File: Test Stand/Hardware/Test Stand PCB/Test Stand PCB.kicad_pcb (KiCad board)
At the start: 2 copper layers, 18 parts, among them J1 Screw_Terminal_01x02, J2 Screw_Terminal_01x02, J3 Screw_Terminal_01x02, J4 Screw_Terminal_01x04, J5 Screw_Terminal_01x02, U1 AdafruitHuzzah32Breakout, U2 Adafruit_MAX31856, U3 Adafruit_MAX31856, U4 Adafruit_MAX31856, U5 Adafruit_MAX31856, U7 INA_122P, U8 Adafruit_MicroSD_Breakout

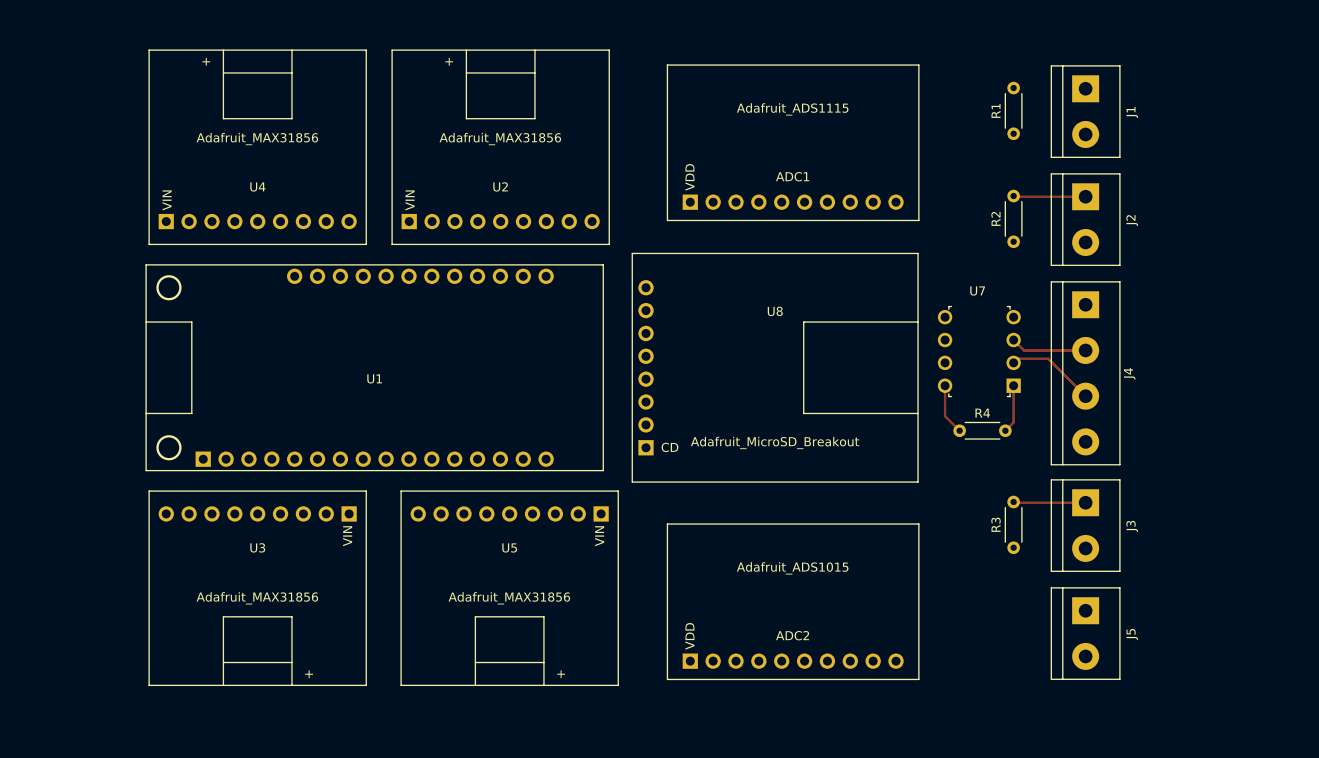
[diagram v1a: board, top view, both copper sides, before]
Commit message: Updated Test schematic and PCB Design
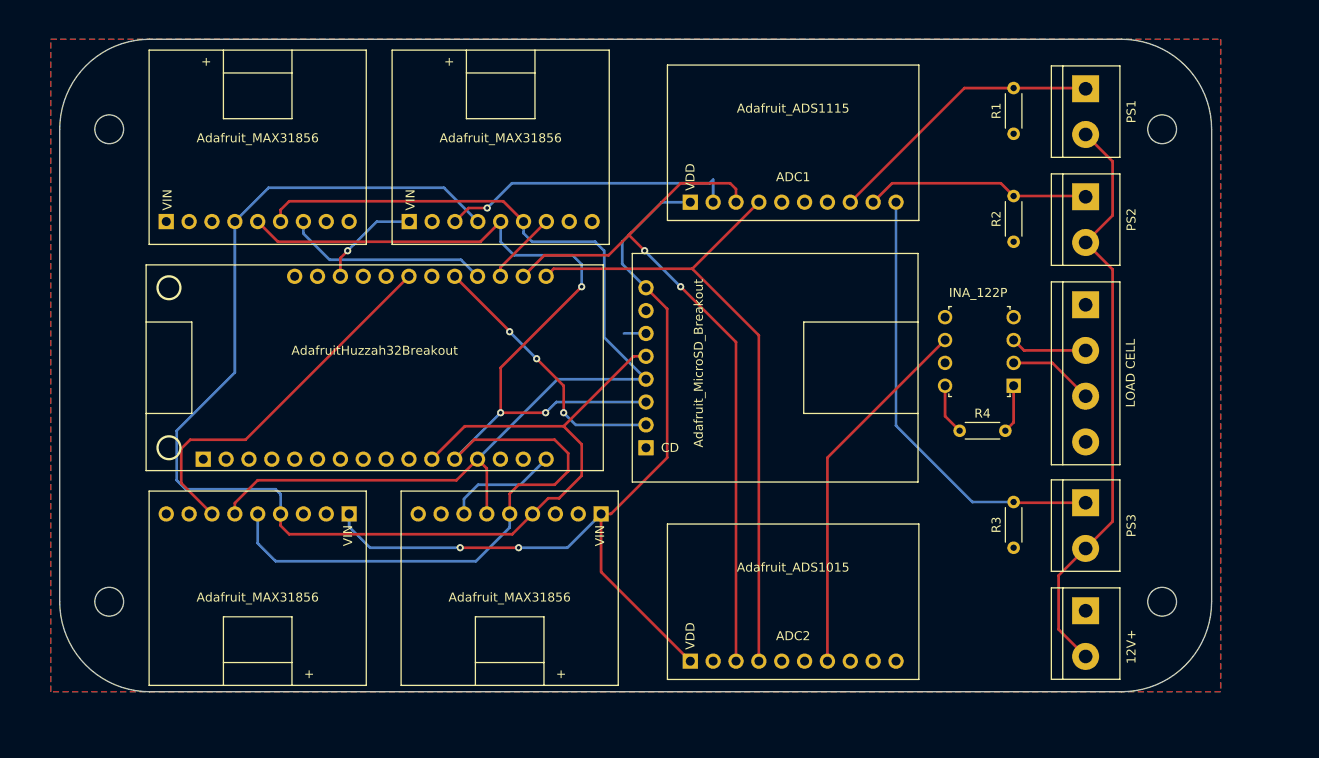
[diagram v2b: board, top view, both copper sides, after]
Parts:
- added G***: LOGO, Test Stand PCB Breakout:Thrust_Logo, B.Cu at (122.5, 82.5)
- added REF**: MountingHole_3.2mm_M3, MountingHole:MountingHole_3.2mm_M3, F.Cu at (163.5, 100.0)
- added REF**: MountingHole_3.2mm_M3, MountingHole:MountingHole_3.2mm_M3, F.Cu at (163.5, 47.5)
- added REF**: MountingHole_3.2mm_M3, MountingHole:MountingHole_3.2mm_M3, F.Cu at (46.5, 100.0)
- added REF**: MountingHole_3.2mm_M3, MountingHole:MountingHole_3.2mm_M3, F.Cu at (46.5, 47.5)
- LOAD CELL: renamed from J4
- R1, R2, R3: value 250 -> 100
- renumbered J5 to 12V+, J1 to PS1, J2 to PS2, J3 to PS3, U4 to U3, U3 to U4
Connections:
- net +9V renamed +12V
- U1 pad 16: Net-(U1-Pad16) -> CS_4
- U1 pad 2: +3V3 -> Net-(U1-Pad2)
- U1 pad 21: CS_3 -> CS_5
- U1 pad 22: CS_4 -> Net-(U1-Pad22)
- U1 pad 23: CS_5 -> CS_3
- U8 pad 7: +3V3 -> Net-(U8-Pad7)
- U8 pad 8: Net-(U8-Pad8) -> +5V
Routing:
- net SPI_SCK: track 0.00 -> 148.6 mm
- net SPI_MOSI: track 0.00 -> 146.3 mm, vias 0 -> 3
- net SPI_MISO: track 0.00 -> 116.0 mm
- net +5V: track 0.00 -> 109.2 mm, vias 0 -> 3
- net I2C_SCL: track 0.00 -> 81.9 mm, vias 0 -> 2
- net I2C_SDA: track 0.00 -> 73.7 mm
- net +12V: track 0.00 -> 65.5 mm
- net CS_3: track 0.00 -> 41.9 mm
- net ADC_A3: track 8.03 -> 49.4 mm
- net LOAD_CELL_VOLTAGE: track 0.00 -> 41.1 mm
- net GND: track 0.00 -> 35.6 mm, vias 0 -> 1
- net ADC_A1: track 0.00 -> 31.4 mm
- net CS_5: track 0.00 -> 29.9 mm, vias 0 -> 3
- net CS_2: track 0.00 -> 22.6 mm
- net ADC_A2: track 8.03 -> 25.2 mm
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- added copper zone on F.Cu, net +5V
- added copper zone on B.Cu, net GND
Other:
- board outline added: 128 x 72.5 mm
- board text added: "THRUST TEAM 3 Channel 4-20mA Pressure Transducer 4 Channel Thermocouple Amplifier 1 Channel Load Cell"

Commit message: Added gerber file for manufacturing of Test Stand PCB v1.0
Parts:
- added D1: D_Schottky, Diode_THT:D_DO-41_SOD81_P7.62mm_Horizontal, F.Cu at (144.0, 87.0)
- added EA1: Screw_Terminal_01x02, TerminalBlock:TerminalBlock_bornier-2_P5.08mm, F.Cu at (146.5, 105.0)
- added Q1: Q_NMOS_GDS, Package_TO_SOT_THT:TO-251-3_Vertical, F.Cu at (143.5, 98.5)
- added R5: 100, Resistor_THT:R_Axial_DIN0204_L3.6mm_D1.6mm_P5.08mm_Horizontal, F.Cu at (140.0, 93.5)
- added R6: 10k, Resistor_THT:R_Axial_DIN0204_L3.6mm_D1.6mm_P5.08mm_Horizontal, F.Cu at (140.0, 91.0)
- +   12V   -: renamed from 12V+
- moved R3 15.1 mm to (149.0, 79.0), turned to 270 degrees
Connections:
- U1 pad 22: Net-(U1-Pad22) -> CS_3
- U1 pad 23: CS_3 -> Gate_Pin
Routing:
- net Gate_Pin: track 0.00 -> 140.1 mm, vias 0 -> 4
- net +12V: track 65.5 -> 87.8 mm
- net Net-(D1-Pad2): track 0.00 -> 12.9 mm
- net Net-(Q1-Pad1): track 0.00 -> 8.95 mm
- net GND: track 35.6 -> 44.1 mm
- net CS_3: track 41.9 -> 44.4 mm
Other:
- board text added: "3 Channel 4-20mA Sensor 4 Channel Thermocouple Amplifier 1 Channel Load Cell 1 Channel Electric Actuator (Mosfet)"
- board text added: "THRUST TEAM December 2020 Rev 1.0"
- board text removed: "THRUST TEAM 3 Channel 4-20mA Pressure Transducer 4 Channel Thermocouple Amplifier 1 Channel Load Cell"

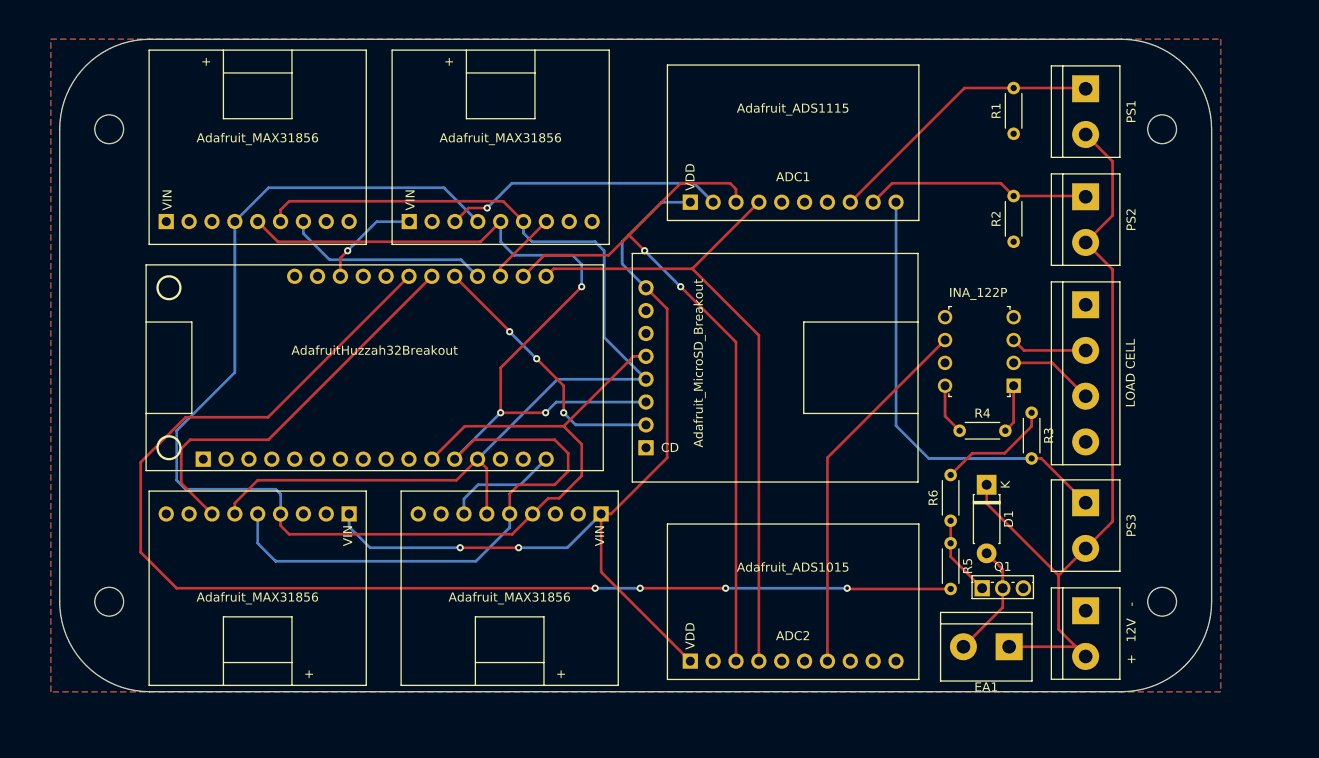
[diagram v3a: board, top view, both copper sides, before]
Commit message: Uploading of the Rev1.1 Board
Rev1.1 Board, changes:
- Added 2 more Electronic actuator circuit drivers
- Changed screw terminal layout
- Added Front and Back Silckscreen
- Improved Layout
- Changed resistor footprint
- Changed Sensor Power from 12V to 24V
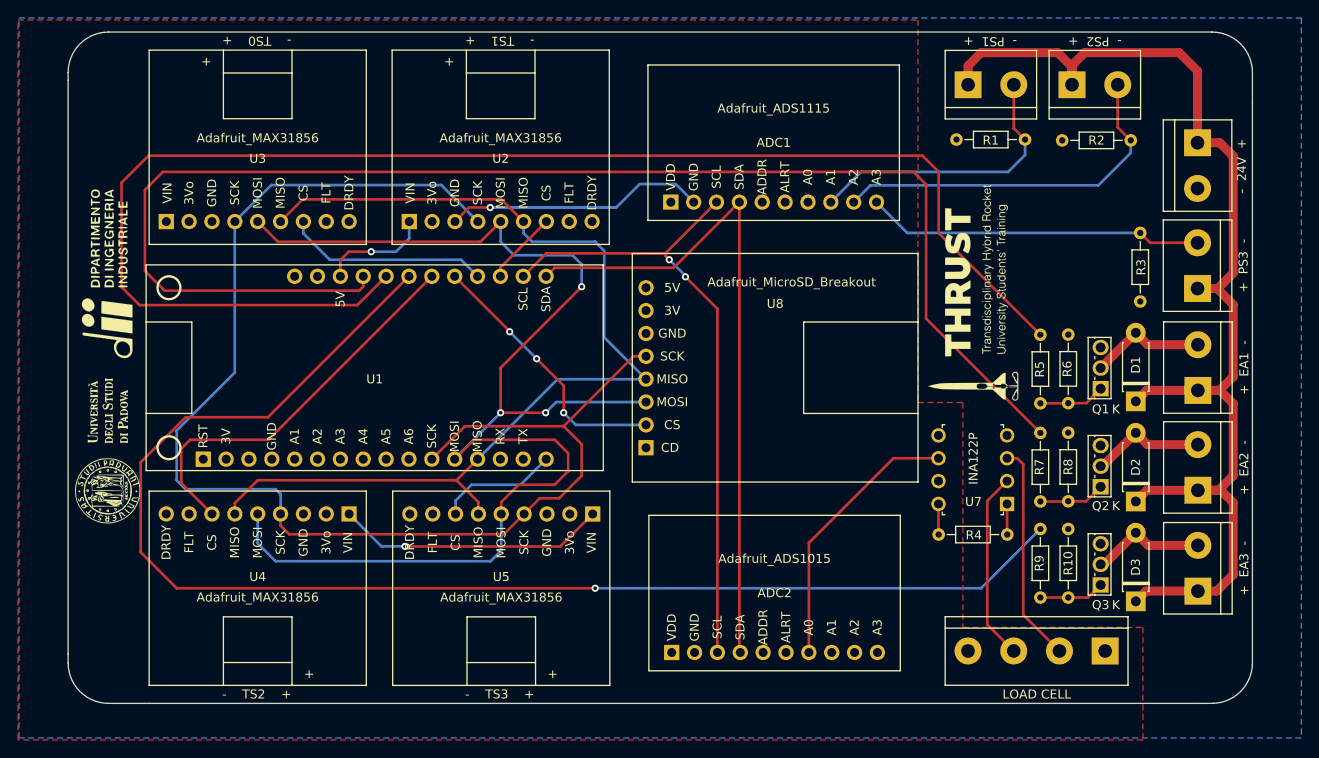
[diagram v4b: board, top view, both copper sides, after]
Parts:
- removed +   12V   -: Screw_Terminal_01x02, TerminalBlock:TerminalBlock_bornier-2_P5.08mm
- removed EA1, PS1, PS2, PS3: Screw_Terminal_01x02, TerminalBlock:TerminalBlock_bornier-2_P5.08mm
- removed REF** (x4): MountingHole_3.2mm_M3, MountingHole:MountingHole_3.2mm_M3
- added +  EA1  -: Screw_Terminal_01x02, TerminalBlock:TerminalBlock_bornier-2_P5.08mm, F.Cu at (167.5, 76.5)
- added +  EA2  -: Screw_Terminal_01x02, TerminalBlock:TerminalBlock_bornier-2_P5.08mm, F.Cu at (167.5, 87.6)
- added +  EA3  -: Screw_Terminal_01x02, TerminalBlock:TerminalBlock_bornier-2_P5.08mm, F.Cu at (167.5, 98.8)
- added +  PS3  -: Screw_Terminal_01x02, TerminalBlock:TerminalBlock_bornier-2_P5.08mm, F.Cu at (167.4, 65.2)
- added -  24V  +: Screw_Terminal_01x02, TerminalBlock:TerminalBlock_bornier-2_P5.08mm, F.Cu at (167.4, 49.0)
- added -  PS1  +: Screw_Terminal_01x02, TerminalBlock:TerminalBlock_bornier-2_P5.08mm, F.Cu at (141.9, 42.5)
- added -  PS2  +: Screw_Terminal_01x02, TerminalBlock:TerminalBlock_bornier-2_P5.08mm, F.Cu at (153.5, 42.5)
- added ?: , , F.Cu at (112.9, 68.5)
- added D2: D_Schottky, Diode_THT:D_DO-41_SOD81_P7.62mm_Horizontal, F.Cu at (160.6, 88.9)
- added D3: D_Schottky, Diode_THT:D_DO-41_SOD81_P7.62mm_Horizontal, F.Cu at (160.6, 100.0)
- added G***: LOGO, Test Stand PCB Breakout:Thrust_Logo_Small, F.Cu at (142.5, 65.7)
- added G***: LOGO, Test Stand PCB Breakout:Dii_logo_small, F.Cu at (46.3, 63.5)
- added G***: LOGO, Test Stand PCB Breakout:Unipd_Logo_small, F.Cu at (46.3, 83.5)
- added Q2: Q_NMOS_GDS, Package_TO_SOT_THT:TO-251-3_Vertical, F.Cu at (156.7, 87.2)
- added Q3: Q_NMOS_GDS, Package_TO_SOT_THT:TO-251-3_Vertical, F.Cu at (156.7, 98.1)
- added R10: 10k, Resistor_THT:R_Axial_DIN0204_L3.6mm_D1.6mm_P7.62mm_Horizontal, F.Cu at (153.1, 99.5)
- added R7: 100, Resistor_THT:R_Axial_DIN0204_L3.6mm_D1.6mm_P7.62mm_Horizontal, F.Cu at (150.0, 81.2)
- added R8: 10k, Resistor_THT:R_Axial_DIN0204_L3.6mm_D1.6mm_P7.62mm_Horizontal, F.Cu at (153.1, 88.8)
- added R9: 100, Resistor_THT:R_Axial_DIN0204_L3.6mm_D1.6mm_P7.62mm_Horizontal, F.Cu at (150.0, 91.9)
- ADC1: footprint Test Bench PCB Breakout:Adafruit_ADS1115 -> Test Stand PCB Breakout:Adafruit_ADS1115
- ADC2: footprint Test Bench PCB Breakout:Adafruit_ADS1015 -> Test Stand PCB Breakout:Adafruit_ADS1015
- R1, R2, R3: value 100 -> 200; footprint Resistor_THT:R_Axial_DIN0204_L3.6mm_D1.6mm_P5.08mm_Horizontal -> Resistor_THT:R_Axial_DIN0204_L3.6mm_D1.6mm_P7.62mm_Horizontal
- R4, R5, R6: footprint Resistor_THT:R_Axial_DIN0204_L3.6mm_D1.6mm_P5.08mm_Horizontal -> Resistor_THT:R_Axial_DIN0204_L3.6mm_D1.6mm_P7.62mm_Horizontal
- U1: footprint Test Bench PCB Breakout:Adafruit_Huzzah32 -> Test Stand PCB Breakout:Adafruit_Huzzah32
- U2, U3, U4, U5: footprint Test Bench PCB Breakout:Adafruit_MAX31856 -> Test Stand PCB Breakout:Adafruit_MAX31856
- U7: footprint Test Bench PCB Breakout:INA_122P -> Test Stand PCB Breakout:INA_122P
- U8: footprint Test Bench PCB Breakout:Adafruit_MicroSD -> Test Stand PCB Breakout:Adafruit_MicroSD
- moved LOAD CELL 38.5 mm to (157.2, 105.5), turned to 180 degrees
- moved Q1 25.8 mm to (156.7, 76.3), turned to 90 degrees
- moved R5 25.2 mm to (150.0, 70.3)
- moved D1 19.0 mm to (160.6, 77.7), turned to 90 degrees
- moved R6 18.5 mm to (153.1, 77.9)
- moved R3 17.3 mm to (161.1, 66.6), turned to 90 degrees
- moved U7 13.2 mm to (146.3, 89.1)
- moved R2 12.5 mm to (152.4, 48.7), turned to 0 degrees
- moved R4 11.8 mm to (138.7, 92.5)
- moved R1 6.39 mm to (140.6, 48.6), turned to 0 degrees
- moved G*** 3.17 mm to (123.5, 79.5)
- moved ADC2 2.28 mm to (120.4, 99.0)
- moved ADC1 2.17 mm to (120.3, 49.0)
- moved U5 0.94 mm to (90.1, 98.5)
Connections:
- D1 pad 1: +12V -> +24V
- LOAD CELL pad 1: GND -> +5V
- LOAD CELL pad 4: +5V -> GND
- R5 pad 1: Net-(Q1-Pad1) -> FET_Gate1
- R5 pad 2: Gate_Pin -> Net-(Q1-Pad1)
- U1 pad 23: Gate_Pin -> FET_Gate3
- U1 pad 24: Net-(U1-Pad24) -> FET_Gate1
- U1 pad 25: Net-(U1-Pad25) -> FET_Gate2
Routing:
- net FET_Gate1: track 0.00 -> 158.7 mm
- net FET_Gate2: track 0.00 -> 156.6 mm
- net FET_Gate3: track 0.00 -> 152.7 mm, vias 0 -> 1
- net +24V: track 0.00 -> 142.3 mm
- net Gate_Pin: track 140.1 -> 0.00 mm, vias 4 -> 0
- net +12V: track 87.8 -> 0.00 mm
- net +5V: track 109.2 -> 42.4 mm, vias 3 -> 2
- net ADC_A2: track 25.2 -> 41.2 mm
- net Net-(J4-Pad2): track 8.48 -> 24.5 mm
- net GND: track 44.1 -> 29.1 mm
- net Net-(D2-Pad2): track 0.00 -> 12.9 mm
- net Net-(D3-Pad2): track 0.00 -> 12.8 mm
- net ADC_A3: track 49.4 -> 37.5 mm
- net Net-(J4-Pad3): track 10.2 -> 21.0 mm
- net LOAD_CELL_VOLTAGE: track 41.1 -> 30.5 mm
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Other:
- board size 128 x 72.5 mm -> 131.6 x 74.6 mm
- board text added: "+ 24V -"
- board text added: "+ PS1 -"
- board text added: "+ PS2 -"
- board text added: "+ VIN+ VIN- -"
- board text added: "- EA1 +"
- board text added: "- EA2 +"
- board text added: "- EA3 +"
- board text added: "- PS3 +"
- board text added: "- TS0 +"
- board text added: "- TS1 +"
- board text added: "- TS2 +"
- board text added: "- TS3 +"
- board text added: "3V"
- board text added: "3Vo"
- board text added: "5V"
- board text added: "A0"
- board text added: "A1"
- board text added: "A2"
- board text added: "A3"
- board text added: "A4"
- board text added: "A5"
- board text added: "ADDR"
- board text added: "ALRT"
- board text added: "CD"
- board text added: "CS"
- board text added: "D1"
- board text added: "D2"
- board text added: "D3"
- board text added: "DRDY"
- board text added: "FLT"
- board text added: "GND"
- board text added: "INA122P"
- board text added: "MISO"
- board text added: "MOSI"
- board text added: "Q1"
- board text added: "Q2"
- board text added: "Q3"
- board text added: "R1"
- board text added: "R10"
- board text added: "R2"
- board text added: "R3"
- board text added: "R4"
- board text added: "R5"
- board text added: "R6"
- board text added: "R7"
- board text added: "R8"
- board text added: "R9"
- board text added: "RST"
- board text added: "RX"
- board text added: "SCK"
- board text added: "SCL"
- board text added: "SDA"
- board text added: "THRUST TEAM Febraury 2021 Rev 1.1"
- board text added: "TX"
- board text added: "VDD"
- board text added: "VIN"
- board text removed: "3 Channel 4-20mA Sensor 4 Channel Thermocouple Amplifier 1 Channel Load Cell 1 Channel Electric Actuator (Mosfet)"
- board text removed: "THRUST TEAM December 2020 Rev 1.0"

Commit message: Added Mounting Holes
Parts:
- added REF**: MountingHole_3.2mm_M3, MountingHole:MountingHole_3.2mm_M3, F.Cu at (168.7, 41.2)
- added REF**: MountingHole_3.2mm_M3, MountingHole:MountingHole_3.2mm_M3, F.Cu at (168.7, 106.7)
- added REF**: MountingHole_3.2mm_M3, MountingHole:MountingHole_3.2mm_M3, F.Cu at (46.6, 106.7)
- added REF**: MountingHole_3.2mm_M3, MountingHole:MountingHole_3.2mm_M3, F.Cu at (46.6, 41.2)
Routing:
- net +24V: track 142.3 -> 139.5 mm
